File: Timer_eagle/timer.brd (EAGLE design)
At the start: 100 x 80 mm, 17 parts, among them IC1 NE555, IC2 4081N, IC3 4518N, IC4 4070N, K1 G5L, Q1 BC548, Q2 TIP120

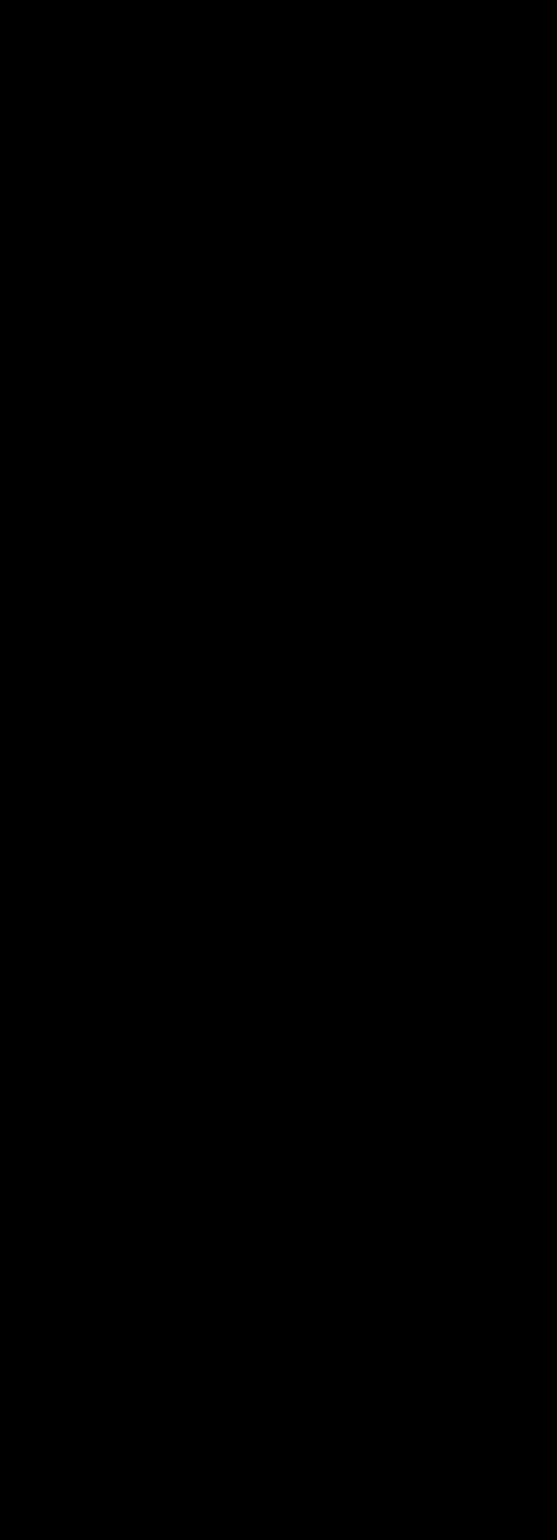
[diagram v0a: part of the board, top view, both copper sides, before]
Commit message: O esquematico do projeto está finalizado
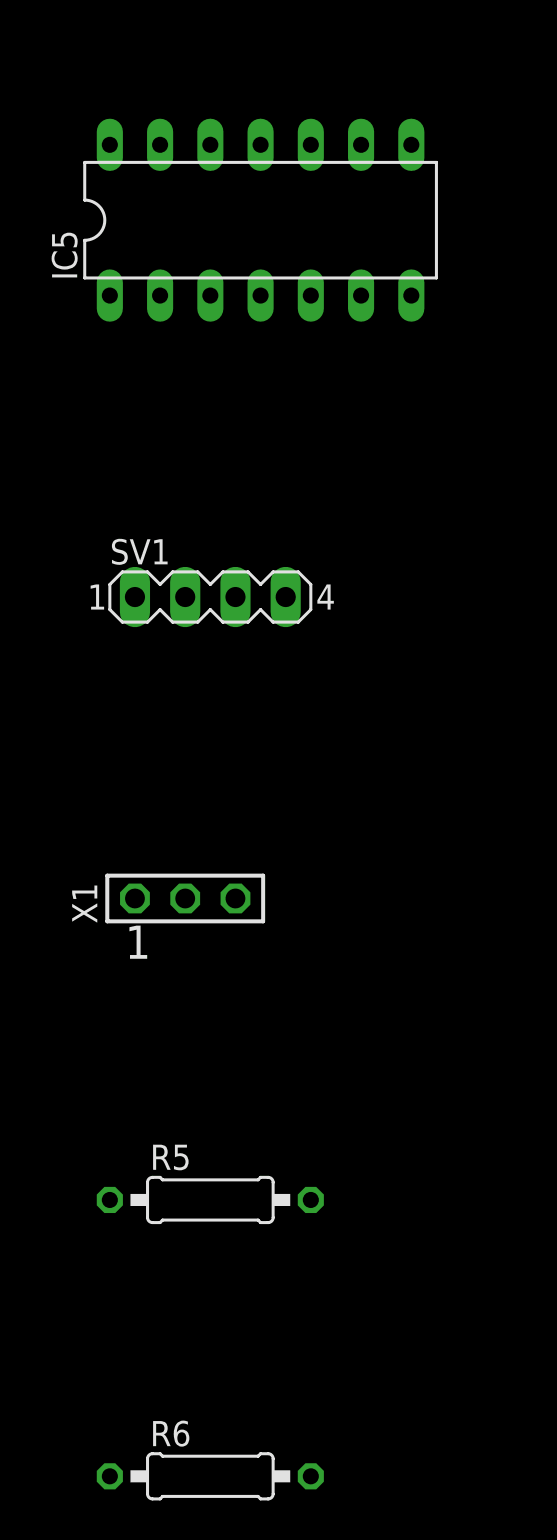
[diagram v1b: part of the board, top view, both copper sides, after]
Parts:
- added IC5: 4070N, 40xx:DIL14
- added R5, R6: (no value), eagle-ltspice:0207/10
- added SV1: (no value), con-lstb:MA04-1
- added X1: SSW-103-02-S-S, con-samtec:SSW-103-02-S-S
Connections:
- removed net VCC+: IC1.8
- new net N$10: IC2.6, IC3.13
- new net N$11: IC2.9, IC3.14
- new net N$12: IC4.3, SV1.1
- new net N$13: IC2.10, IC4.9, IC5.9
- new net N$14: IC4.10, IC5.10, SV1.3
- new net N$15: IC4.4, SV1.2
- new net N$16: D1.A, K1.2
- new net N$17: IC2.3, IC4.2
- new net N$18: IC2.4, IC4.6
- new net N$19: K1.P, X1.2
- new net N$20: X1.1
- new net N$21: K1.O, X1.3
- new net N$22: Q1.B
- new net N$23: LED1.A, R6.2
- new net N$24: R6.1
- new net N$5: R1.2, SW1.4
- new net N$8: IC2.1, IC2.8, IC3.11
- new net N$9: IC2.2, IC2.5, IC3.12
- new net RESET_555: IC1.4, IC3.10, IC3.6, R3.1, R5.1, SV1.4
- net GND: now also Q2.E
- net N$3: now also Q2.B, R3.2; no longer IC3.10, IC3.6
- net VCC: now also D1.C, IC1.8, IC4.1, IC4.5, IC4.8, IC5.8, K1.1, Q1.C
- net VDD: now also IC5.14
- net VSS: now also IC5.7

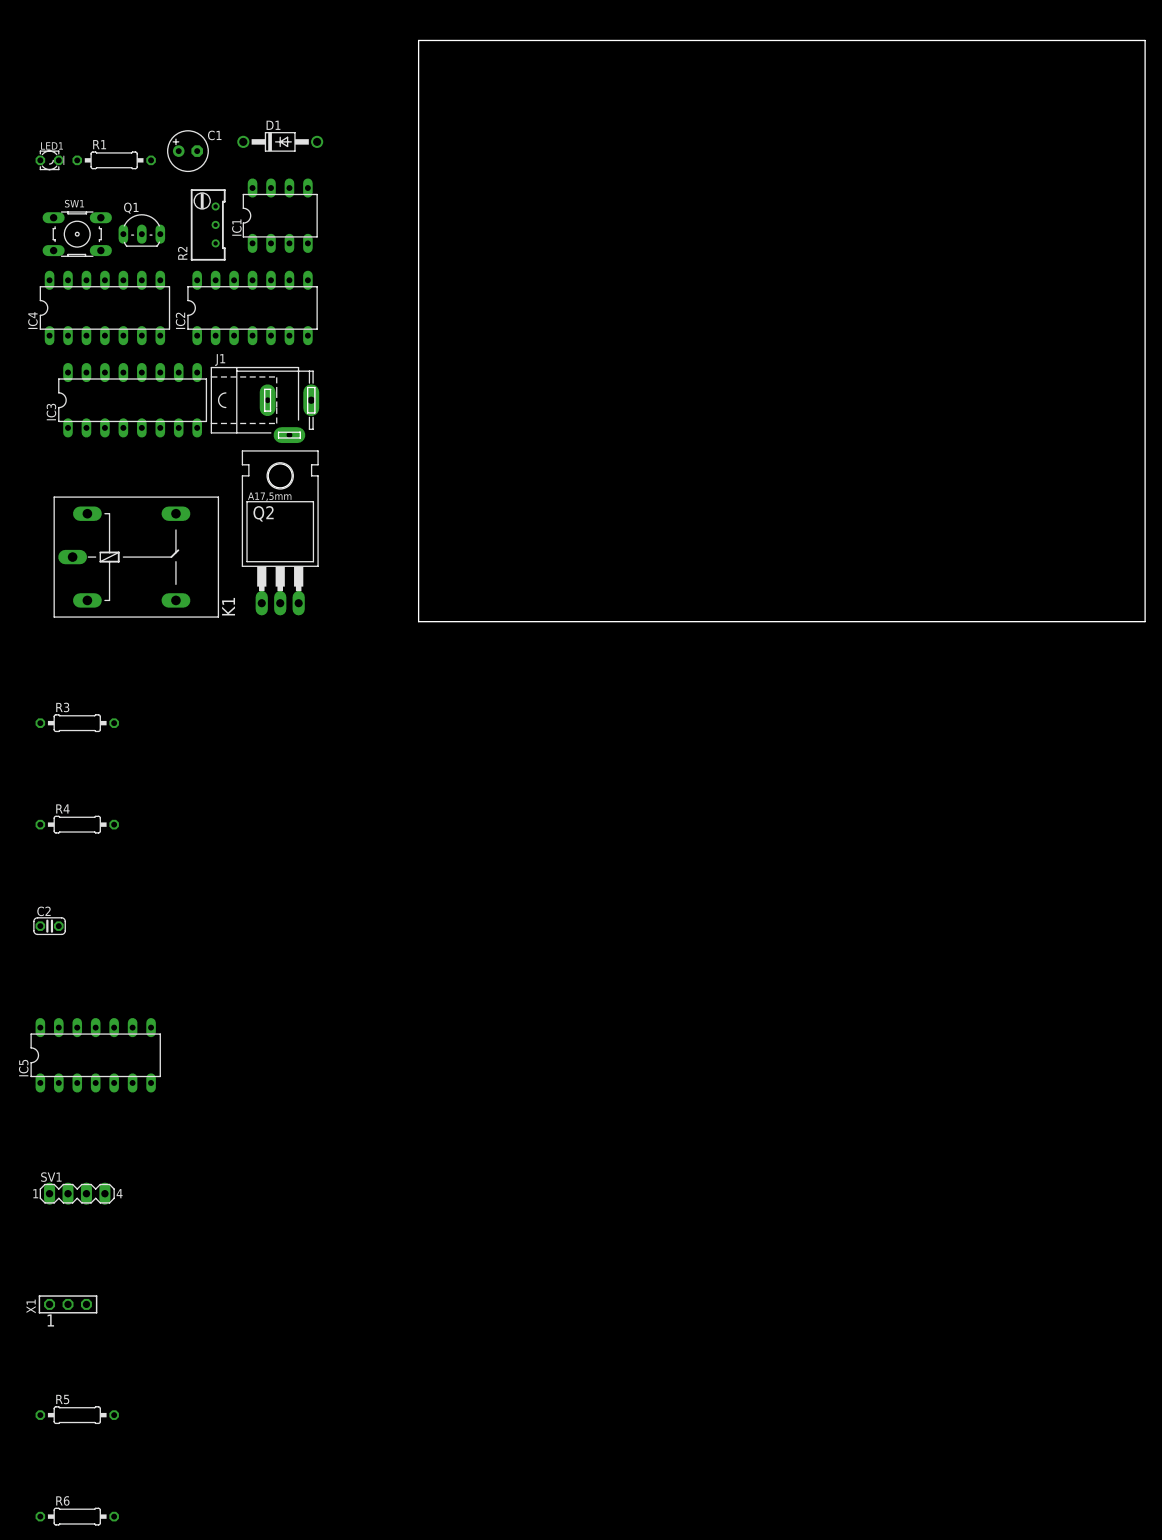
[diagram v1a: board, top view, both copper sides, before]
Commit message: Alguns erros no esquemático foram consertados
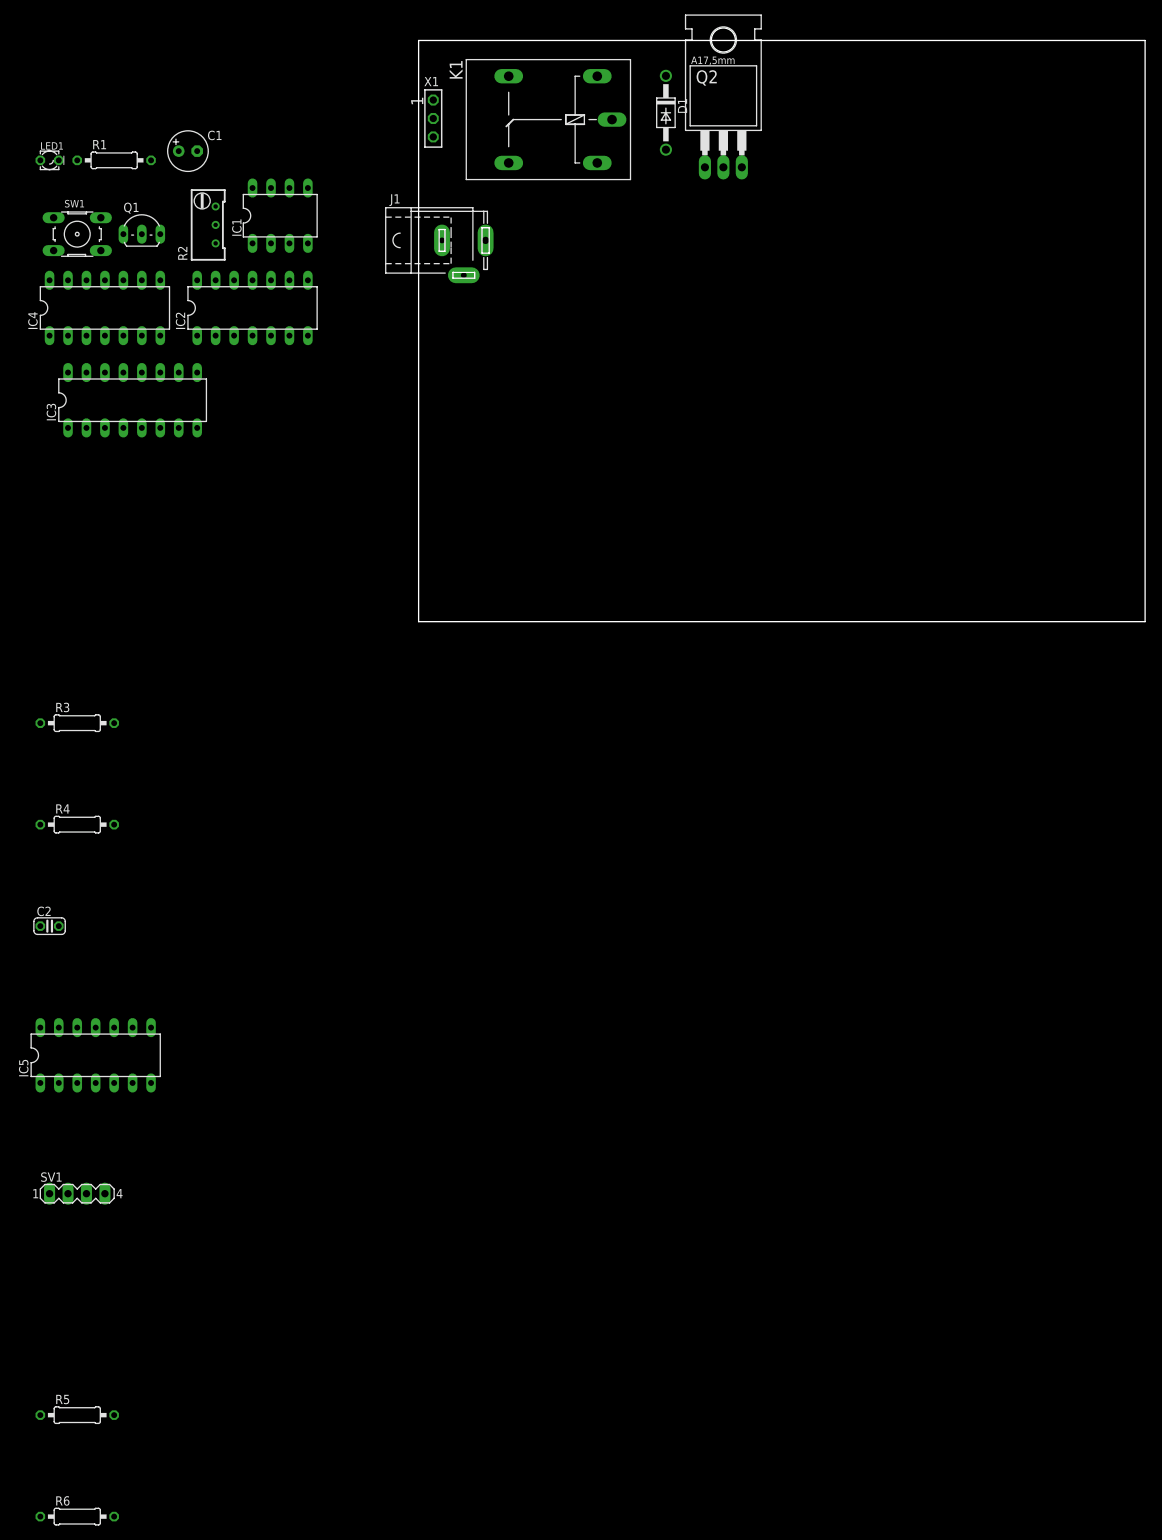
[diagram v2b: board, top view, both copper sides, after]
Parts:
- moved X1 170.8 mm to (2.02, 69.3), turned to 270 degrees
- moved Q2 85.6 mm to (42.0, 68.9)
- moved K1 81.7 mm to (17.1, 69.1), turned to 180 degrees
- moved D1 53.2 mm to (34.0, 70.0), turned to 270 degrees
- moved J1 32.6 mm to (6.22, 52.5)
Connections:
- net N$20: now also K1.S
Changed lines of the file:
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@@
 <setting verticaltext="up"/>
 </settings>
-<grid distance="0.05" unitdist="inch" unit="inch" style="lines" multiple="1" display="no" altdistance="0.025" altunitdist="inch" altunit="inch"/>
+<grid distance="1" unitdist="mm" unit="mm" style="lines" multiple="1" display="no" altdistance="0.025" altunitdist="inch" altunit="inch"/>
 <layers>
 <layer number="1" name="Top" color="4" fill="1" visible="yes" active="yes"/>
@@
 <wire x1="100" y1="80" x2="0" y2="80" width="0" layer="20"/>
 <wire x1="0" y1="80" x2="0" y2="0" width="0" layer="20"/>
+<dimension x1="0" y1="80" x2="50" y2="80" x3="25" y3="81" textsize="1.778" layer="16"/>
+<dimension x1="0" y1="80" x2="0" y2="-20" x3="-1" y3="30" textsize="1.27" layer="16"/>
+<dimension x1="0" y1="80" x2="0" y2="30" x3="2" y3="55" textsize="1.27" layer="16"/>
 </plain>
 <attributes>
@@
 <elements>
 <element name="C1" library="rcl" package="E2,5-6" value="" x="-31.75" y="64.77"/>
-<element name="D1" library="diode" package="DO41-10" value="1N4004" x="-19.05" y="66.04"/>
+<element name="D1" library="diode" package="DO41-10" value="1N4004" x="34.04" y="70.05" rot="R270"/>
 <element name="IC1" library="st-microelectronics" package="DIL-08" value="NE555" x="-19.05" y="55.88">
 <attribute name="OC_FARNELL" value="1467742" x="-19.05" y="55.88" size="1.778" layer="27" display="off"/>
@@
 <element name="IC3" library="45xx" package="DIL16" value="4518N" x="-39.37" y="30.48"/>
 <element name="IC4" library="40xx" package="DIL14" value="4070N" x="-43.18" y="43.18"/>
-<element name="J1" library="con-jack" package="SPC4077" value="" x="-17.78" y="30.48">
-<attribute name="OC_FARNELL" value="unknown" x="-17.78" y="30.48" size="1.778" layer="27" display="off"/>
-<attribute name="MPN" value="" x="-17.78" y="30.48" size="1.778" layer="27" display="off"/>
-<attribute name="OC_NEWARK" value="unknown" x="-17.78" y="30.48" size="1.778" layer="27" display="off"/>
-<attribute name="MF" value="" x="-17.78" y="30.48" size="1.778" layer="27" display="off"/>
-</element>
-<element name="K1" library="relay" package="G5LE" value="G5L" x="-38.1" y="8.89">
-<attribute name="OC_FARNELL" value="unknown" x="-38.1" y="8.89" size="1.778" layer="27" display="off"/>
-<attribute name="MPN" value="" x="-38.1" y="8.89" size="1.778" layer="27" display="off"/>
-<attribute name="OC_NEWARK" value="unknown" x="-38.1" y="8.89" size="1.778" layer="27" display="off"/>
-<attribute name="MF" value="" x="-38.1" y="8.89" size="1.778" layer="27" display="off"/>
+<element name="J1" library="con-jack" package="SPC4077" value="" x="6.22" y="52.48">
+<attribute name="OC_FARNELL" value="unknown" x="6.22" y="52.48" size="1.778" layer="27" display="off"/>
+<attribute name="MPN" value="" x="6.22" y="52.48" size="1.778" layer="27" display="off"/>
+<attribute name="OC_NEWARK" value="unknown" x="6.22" y="52.48" size="1.778" layer="27" display="off"/>
+<attribute name="MF" value="" x="6.22" y="52.48" size="1.778" layer="27" display="off"/>
+</element>
+<element name="K1" library="relay" package="G5LE" value="G5L" x="17.1" y="69.11" rot="R180">
+<attribute name="OC_FARNELL" value="unknown" x="17.1" y="69.11" size="1.778" layer="27" rot="R180" display="off"/>
+<attribute name="MPN" value="" x="17.1" y="69.11" size="1.778" layer="27" rot="R180" display="off"/>
+<attribute name="OC_NEWARK" value="unknown" x="17.1" y="69.11" size="1.778" layer="27" rot="R180" display="off"/>
+<attribute name="MF" value="" x="17.1" y="69.11" size="1.778" layer="27" rot="R180" display="off"/>
 </element>
 <element name="LED1" library="eagle-ltspice" package="LED_LD260" value="" x="-50.8" y="63.5">
@@
 </element>
 <element name="Q1" library="transistor-npn" package="TO92-EBC" value="BC548" x="-38.1" y="54.61"/>
-<element name="Q2" library="transistor-power" package="TO220AH" value="TIP120" x="-19.05" y="8.89"/>
+<element name="Q2" library="transistor-power" package="TO220AH" value="TIP120" x="41.95" y="68.89"/>
 <element name="R1" library="eagle-ltspice" package="0207/10" value="10k" x="-41.91" y="63.5">
 <attribute name="SPICEMODEL" value="NONE" x="-41.91" y="63.5" size="1.778" layer="27" display="off"/>
@@
 <attribute name="OC_NEWARK" value="unknown" x="-46.99" y="-78.74" size="1.778" layer="27" display="off"/>
 </element>
-<element name="X1" library="con-samtec" package="SSW-103-02-S-S" value="SSW-103-02-S-S" x="-48.26" y="-93.98">
-<attribute name="MF" value="" x="-48.26" y="-93.98" size="1.778" layer="27" display="off"/>
-<attribute name="MPN" value="SSW-103-02-S-S" x="-48.26" y="-93.98" size="1.778" layer="27" display="off"/>
-<attribute name="OC_FARNELL" value="unknown" x="-48.26" y="-93.98" size="1.778" layer="27" display="off"/>
-<attribute name="OC_NEWARK" value="11P9367" x="-48.26" y="-93.98" size="1.778" layer="27" display="off"/>
+<element name="X1" library="con-samtec" package="SSW-103-02-S-S" value="SSW-103-02-S-S" x="2.02" y="69.26" rot="R270">
+<attribute name="MF" value="" x="2.02" y="69.26" size="1.778" layer="27" rot="R270" display="off"/>
+<attribute name="MPN" value="SSW-103-02-S-S" x="2.02" y="69.26" size="1.778" layer="27" rot="R270" display="off"/>
+<attribute name="OC_FARNELL" value="unknown" x="2.02" y="69.26" size="1.778" layer="27" rot="R270" display="off"/>
+<attribute name="OC_NEWARK" value="11P9367" x="2.02" y="69.26" size="1.778" layer="27" rot="R270" display="off"/>
 </element>
 <element name="R5" library="eagle-ltspice" package="0207/10" value="" x="-46.99" y="-109.22">
@@
 <contactref element="C2" pad="2"/>
 <contactref element="Q2" pad="E"/>
-<wire x1="-16.51" y1="2.54" x2="-49.53" y2="-41.91" width="0" layer="19" extent="1-1"/>
-<wire x1="-17.78" y1="25.68" x2="-16.51" y2="2.54" width="0" layer="19" extent="1-1"/>
-<wire x1="-20.78" y1="30.48" x2="-17.78" y2="25.68" width="0" layer="19" extent="1-1"/>
-<wire x1="-30.48" y1="34.29" x2="-20.78" y2="30.48" width="0" layer="19" extent="1-1"/>
+<wire x1="44.49" y1="62.54" x2="-49.53" y2="-41.91" width="0" layer="19" extent="1-1"/>
+<wire x1="6.22" y1="47.68" x2="44.49" y2="62.54" width="0" layer="19" extent="1-1"/>
+<wire x1="3.22" y1="52.48" x2="6.22" y2="47.68" width="0" layer="19" extent="1-1"/>
+<wire x1="-30.48" y1="34.29" x2="3.22" y2="52.48" width="0" layer="19" extent="1-1"/>
 <wire x1="-22.86" y1="52.07" x2="-30.48" y2="34.29" width="0" layer="19" extent="1-1"/>
 <wire x1="-30.48" y1="64.77" x2="-22.86" y2="52.07" width="0" layer="19" extent="1-1"/>
@@
 <wire x1="-50.8" y1="46.99" x2="-48.26" y2="34.29" width="0" layer="19" extent="1-1"/>
 <wire x1="-30.48" y1="46.99" x2="-50.8" y2="46.99" width="0" layer="19" extent="1-1"/>
-<wire x1="-14.78" y1="30.48" x2="-30.48" y2="46.99" width="0" layer="19" extent="1-1"/>
+<wire x1="9.22" y1="52.48" x2="-30.48" y2="46.99" width="0" layer="19" extent="1-1"/>
 </signal>
 <signal name="N$1">
@@
 <contactref element="Q1" pad="C"/>
 <wire x1="-41.91" y1="-27.94" x2="-36.83" y2="-55.88" width="0" layer="19" extent="1-1"/>
-<wire x1="-45.593" y1="2.921" x2="-41.91" y2="-27.94" width="0" layer="19" extent="1-1"/>
-<wire x1="-40.64" y1="39.37" x2="-45.593" y2="2.921" width="0" layer="19" extent="1-1"/>
+<wire x1="24.593" y1="75.079" x2="-41.91" y2="-27.94" width="0" layer="19" extent="1-1"/>
+<wire x1="-40.64" y1="39.37" x2="24.593" y2="75.079" width="0" layer="19" extent="1-1"/>
 <wire x1="-35.56" y1="46.99" x2="-40.64" y2="39.37" width="0" layer="19" extent="1-1"/>
 <wire x1="-40.64" y1="53.34" x2="-35.56" y2="46.99" width="0" layer="19" extent="1-1"/>
@@
 <wire x1="-50.8" y1="39.37" x2="-40.64" y2="39.37" width="0" layer="19" extent="1-1"/>
 <wire x1="-22.86" y1="59.69" x2="-35.56" y2="46.99" width="0" layer="19" extent="1-1"/>
-<wire x1="-24.13" y1="66.04" x2="-22.86" y2="59.69" width="0" layer="19" extent="1-1"/>
+<wire x1="34.04" y1="75.13" x2="-22.86" y2="59.69" width="0" layer="19" extent="1-1"/>
 </signal>
 <signal name="N$2">
@@
 <contactref element="Q2" pad="B"/>
 <contactref element="R3" pad="2"/>
-<wire x1="-21.59" y1="2.54" x2="-41.91" y2="-13.97" width="0" layer="19" extent="1-1"/>
+<wire x1="39.41" y1="62.54" x2="-41.91" y2="-13.97" width="0" layer="19" extent="1-1"/>
 </signal>
 <signal name="N$16">
 <contactref element="K1" pad="2"/>
 <contactref element="D1" pad="A"/>
-<wire x1="-45.593" y1="14.859" x2="-13.97" y2="66.04" width="0" layer="19" extent="1-1"/>
+<wire x1="24.593" y1="63.141" x2="34.04" y2="64.97" width="0" layer="19" extent="1-1"/>
 </signal>
 <signal name="N$19">
 <contactref element="X1" pad="2"/>
 <contactref element="K1" pad="P"/>
-<wire x1="-47.625" y1="8.89" x2="-48.26" y2="-93.98" width="0" layer="19" extent="1-1"/>
+<wire x1="26.625" y1="69.11" x2="2.02" y2="69.26" width="0" layer="19" extent="1-1"/>
 </signal>
 <signal name="N$20">
 <contactref element="X1" pad="1"/>
+<contactref element="K1" pad="S"/>
+<wire x1="12.401" y1="75.079" x2="2.02" y2="71.8" width="0" layer="19" extent="1-1"/>
 </signal>
 <signal name="N$21">
 <contactref element="X1" pad="3"/>
 <contactref element="K1" pad="O"/>
-<wire x1="-33.401" y1="14.859" x2="-45.72" y2="-93.98" width="0" layer="19" extent="1-1"/>
+<wire x1="12.401" y1="63.141" x2="2.02" y2="66.72" width="0" layer="19" extent="1-1"/>
 </signal>
 <signal name="N$22">
